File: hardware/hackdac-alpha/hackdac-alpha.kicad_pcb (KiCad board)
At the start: 4 copper layers, 120 x 75 mm, 205 parts, among them J1 VIDEO OUT, J10 HOLE, J11 HOLE, J12 HOLE, J13 HOLE, J2 TTL SYNC, J3 SYNC OUT, J4 I2C, J5 AUDIO OUT, J6 EXT LEDS, J7 EXT POWER, J8 HOLE, J9 HOLE, P1 BANK2_AUX, P2 P22, P3 P28, P4 P20, Q1 2N7002, Q2 BC847, Q3 BC857, Q4 BC857, Q5 2N7002, Q6 2N7002, Q7 IRLML2244, U1 AD768, U10 74LVC1G07, U11 TPS61170DRVR, U12 TPS63700DRCT, U2 MAX4104, U3 TLE2082, U4 MAX4104, U5 MCP47FEB22A1-E/ST, U6 74LVCH16T245, U7 74LVC1G125, U8 MCP1700T-3302E/MB, U9 PCM5102, X1 ECS-TXO-3225-270-TR

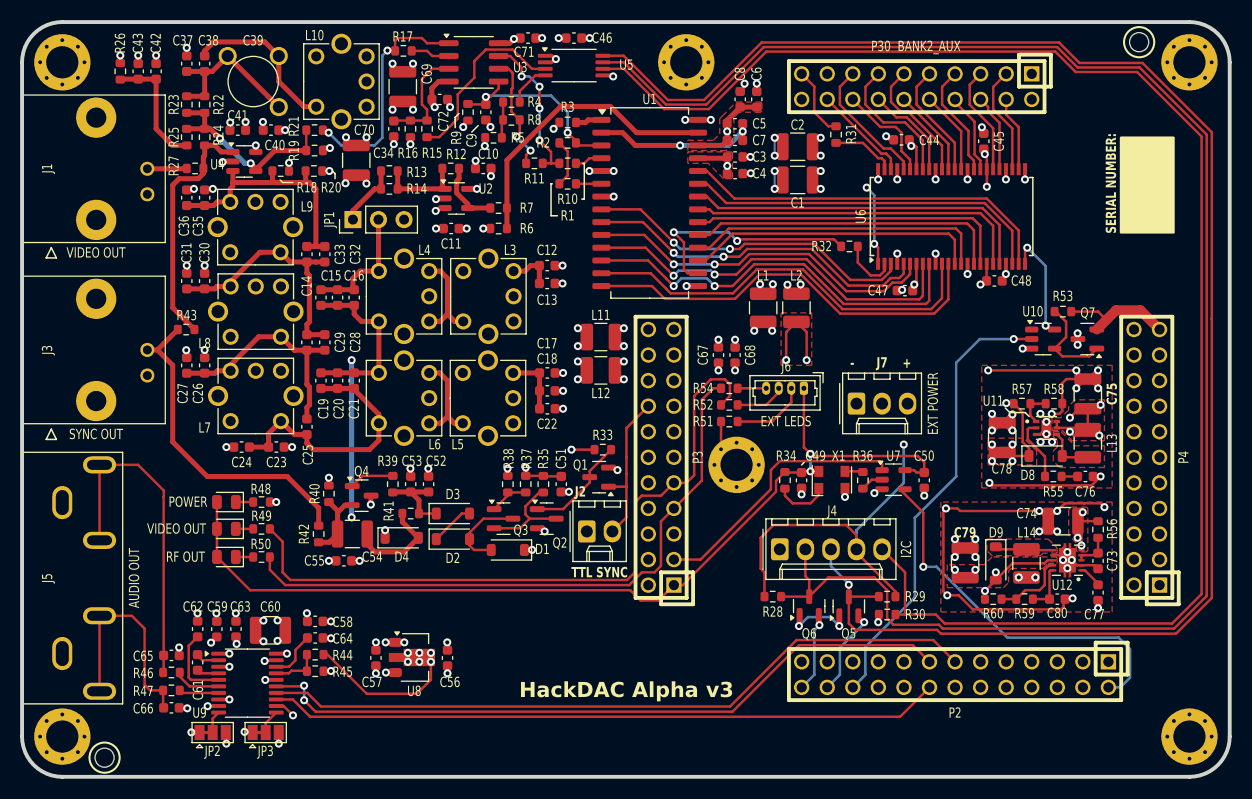
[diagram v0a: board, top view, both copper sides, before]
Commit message: More PCB layout for V3, update readme
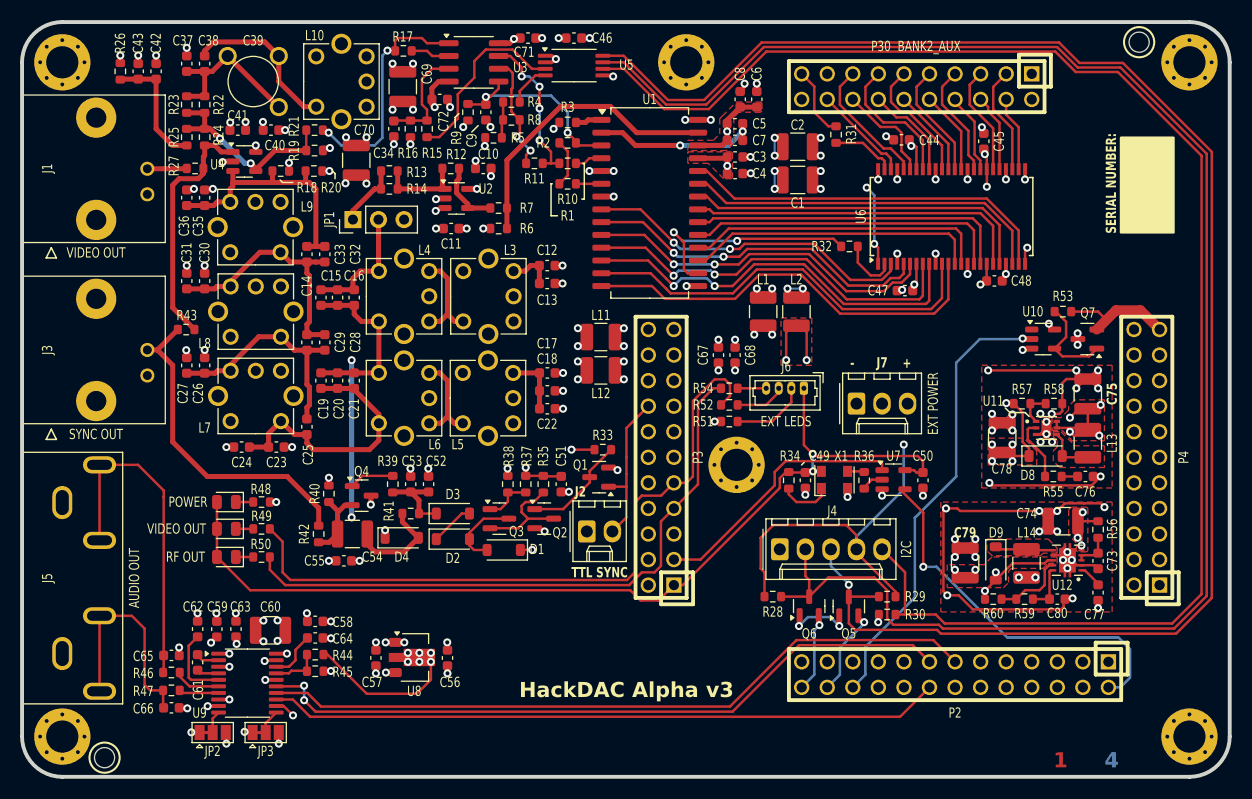
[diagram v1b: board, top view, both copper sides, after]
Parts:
- moved D1 0.41 mm to (127.6, 116.2)
- moved Q3 0.41 mm to (127.1, 113.1)
- moved C49 0.38 mm to (157.5, 109.3)
- moved R34 0.38 mm to (155.9, 109.3)
- moved L1 0.38 mm to (153.4, 92.5)
- moved L2 0.38 mm to (156.7, 92.5)
- moved Q2 0.25 mm to (131.6, 113.1)
- moved X1 0.25 mm to (160.4, 109.2)
- moved C50 0.13 mm to (169.2, 109.3)
- moved R36 0.13 mm to (163.4, 109.3)
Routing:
- net GND: track 1068.2 -> 1071.9 mm, vias 140 -> 141
- net VIN: track 144.8 -> 143.1 mm
- net /video/ADAC-: track 38.1 -> 39.3 mm
- net DA_SDA: track 163.7 -> 162.6 mm
- net DA_HVC: track 151.9 -> 150.8 mm
- net DA_SCL: track 166.6 -> 165.5 mm
- net +5V: track 167.0 -> 168.1 mm
- net /video/ADAC+: track 28.0 -> 29.1 mm
- net Net-(Q3-B): track 4.00 -> 4.78 mm
- net +3.3V_HACKRF: track 291.9 -> 291.2 mm
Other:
- board text added: "1"
- board text added: "2"
- board text added: "3"
- board text added: "4"

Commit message: Modify I2C buffering to allow power-down of HackDAC
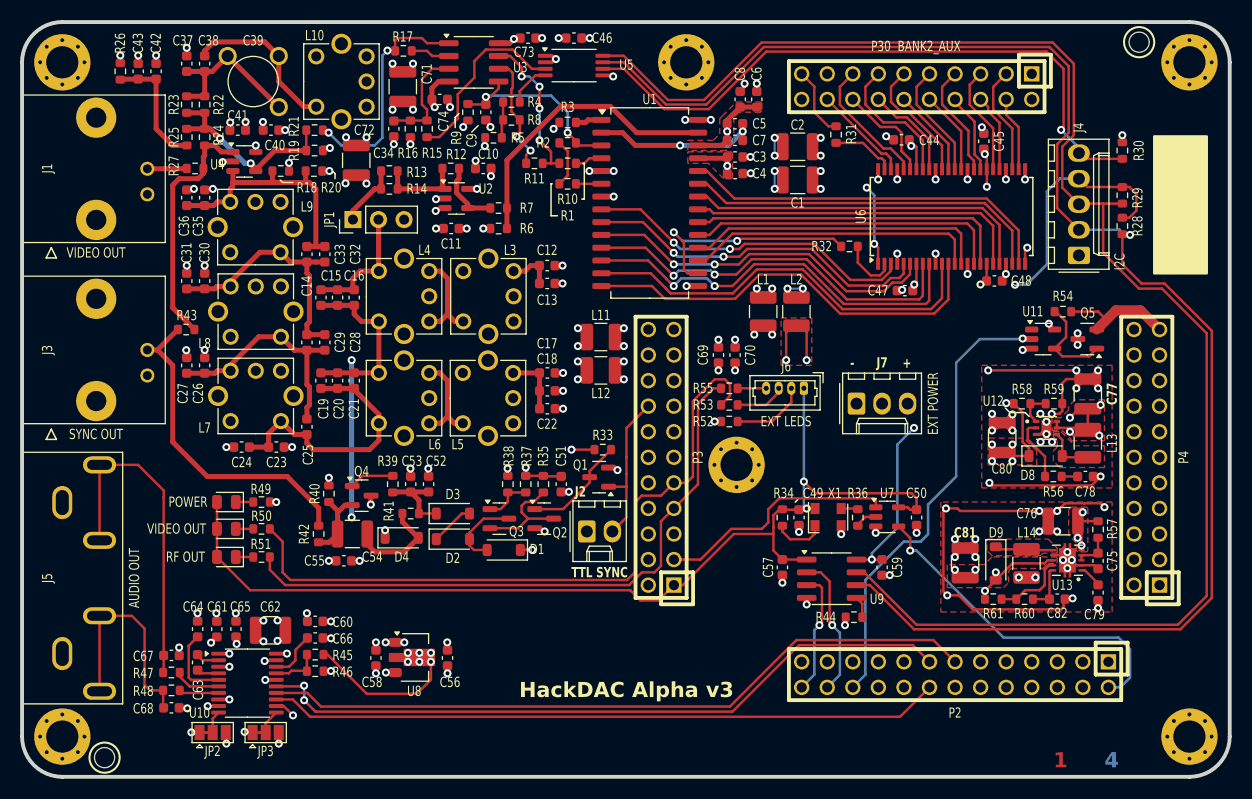
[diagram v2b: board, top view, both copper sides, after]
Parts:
- removed the Q5 at (161.9, 121.8)
- removed Q6: 2N7002, Package_TO_SOT_SMD:SOT-23
- added C57: 100n, Capacitor_SMD:C_0603_1608Metric, F.Cu at (155.3, 117.9)
- added C59: 100n, Capacitor_SMD:C_0603_1608Metric, F.Cu at (165.2, 117.9)
- added R44: NF, Resistor_SMD:R_0603_1608Metric, F.Cu at (162.4, 122.9)
- added U9: TCA9517D, Package_SO:SOIC-8_3.9x4.9mm_P1.27mm, F.Cu at (160.2, 119.1)
- R13, R20: value NF -> 100
- R14, R18: value 50 -> 100
- moved R30 51.7 mm to (189.0, 76.5), turned to 90 degrees
- moved R28 50.6 mm to (189.0, 84.0), turned to -90 degrees
- moved R29 46.2 mm to (189.0, 81.0), turned to -90 degrees
- moved J4 41.7 mm to (184.7, 86.9), turned to 90 degrees
- moved U7 3.75 mm to (165.7, 112.9)
- moved C49 3.75 mm to (156.9, 113.0)
- moved R34 3.75 mm to (155.3, 113.0)
- moved R36 3.75 mm to (162.8, 113.0)
- moved X1 3.75 mm to (159.8, 112.9)
- moved C50 3.75 mm to (168.6, 113.0)
- renumbered C57 to C58, C58 to C60, C59 to C61, C60 to C62, C61 to C63, C62 to C64, C63 to C65, C64 to C66, C65 to C67, C66 to C68, C67 to C69, C68 to C70, C69 to C71, C70 to C72, C71 to C73, C72 to C74, C73 to C75, C74 to C76, C75 to C77, C76 to C78, C77 to C79, C78 to C80, C79 to C81, C80 to C82, Q7 to Q5, R44 to R45, R45 to R46, R46 to R47, R47 to R48, R48 to R49, R49 to R50, R50 to R51, R51 to R52, R52 to R53, R53 to R54, R54 to R55, R55 to R56, R56 to R57, R57 to R58, R58 to R59, R59 to R60, R60 to R61, U9 to U10, U10 to U11, U11 to U12, U12 to U13
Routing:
- net DA_HVC: track 150.8 -> 64.3 mm, vias 0 -> 1
- net GND: track 1071.9 -> 1133.3 mm, vias 141 -> 145
- net DA_SCL: track 165.5 -> 154.5 mm, vias 0 -> 1
- net DA_SDA: track 162.6 -> 154.1 mm, vias 1 -> 0
- net +5V: track 168.1 -> 175.4 mm, vias 15 -> 17
- net /audio/SDA: track 8.87 -> 14.1 mm
- net /audio/SCL: track 7.90 -> 12.5 mm
- net TCXO_CLK: track 38.0 -> 34.7 mm
- net TCXO_ENABLE: track 26.3 -> 24.1 mm
- net Net-(U9-EN): track 0.00 -> 2.16 mm
- net PWR_EN: track 45.0 -> 46.0 mm
- net VIN: track 143.1 -> 143.7 mm
- net +3.3V_HACKRF: track 291.2 -> 291.5 mm, vias 11 -> 9
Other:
- board text removed: "SERIAL NUMBER:"

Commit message: Move LEDs underneath lightpipes
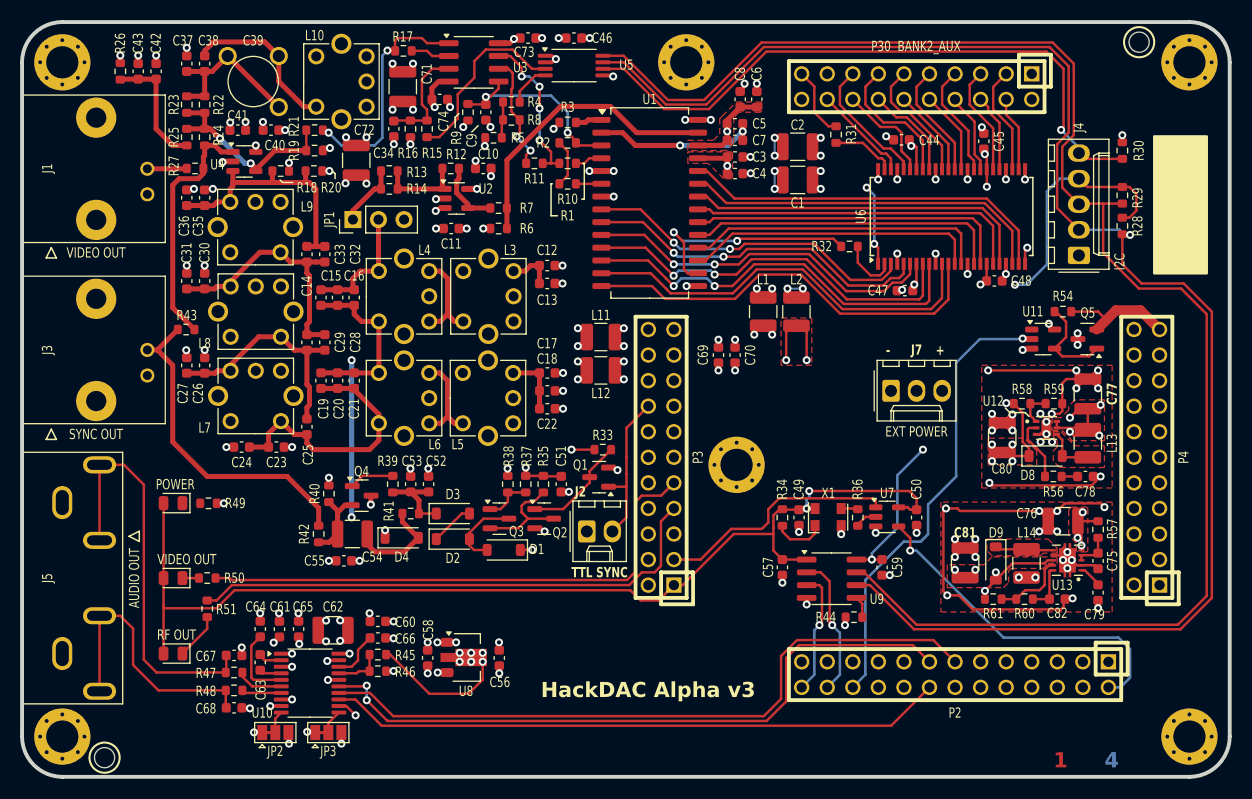
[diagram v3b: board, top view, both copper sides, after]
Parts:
- removed J6: EXT LEDS, Connector_Molex:Molex_PicoBlade_53047-0410_1x04_P1.25mm_Vertical
- removed R52, R53, R55: 100, Resistor_SMD:R_0603_1608Metric
- moved D7 11.0 mm to (94.7, 126.5)
- moved R51 7.46 mm to (98.1, 122.0), turned to -90 degrees
- moved R50 7.28 mm to (98.1, 119.0)
- moved D6 7.21 mm to (94.7, 119.0)
- moved C60 6.22 mm to (115.1, 123.3)
- moved C61 6.22 mm to (105.3, 124.1)
- moved C62 6.22 mm to (110.6, 124.2)
- moved C63 6.22 mm to (103.4, 127.4)
- moved C64 6.22 mm to (103.4, 124.1)
- moved C65 6.22 mm to (107.2, 124.1)
- moved C66 6.22 mm to (115.1, 125.0)
- moved C67 6.22 mm to (100.8, 126.7)
- moved C68 6.22 mm to (100.8, 131.9)
- moved JP2 6.22 mm to (104.9, 134.3)
- moved JP3 6.22 mm to (110.1, 134.3)
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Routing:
- net /power/VIDEO_OUT_LED: track 68.9 -> 53.7 mm
- net /power/RF_OUT_LED: track 62.1 -> 52.8 mm
- net Net-(J6-Pin_2): track 7.52 -> 0.00 mm
- net +5V: track 175.4 -> 168.0 mm
- net Net-(J5-IN2): track 33.1 -> 40.5 mm
- net GND: track 1133.3 -> 1139.6 mm, vias 145 -> 144
- net /audio/I2S_SCK: track 66.8 -> 61.3 mm
- net Net-(J5-IN1): track 21.9 -> 27.0 mm
- net Net-(J6-Pin_3): track 5.00 -> 0.00 mm
- net -5V: track 66.1 -> 70.3 mm
- net +3.3V_HACKRF: track 291.5 -> 294.7 mm
- net /audio/I2S_SDA: track 71.6 -> 68.7 mm
- net /audio/I2S_WS: track 70.3 -> 67.4 mm
- net Net-(D7-K): track 1.73 -> 4.65 mm
- net Net-(J6-Pin_4): track 2.83 -> 0.00 mm
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
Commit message: Changed X1 to 5x3.2mm footprint
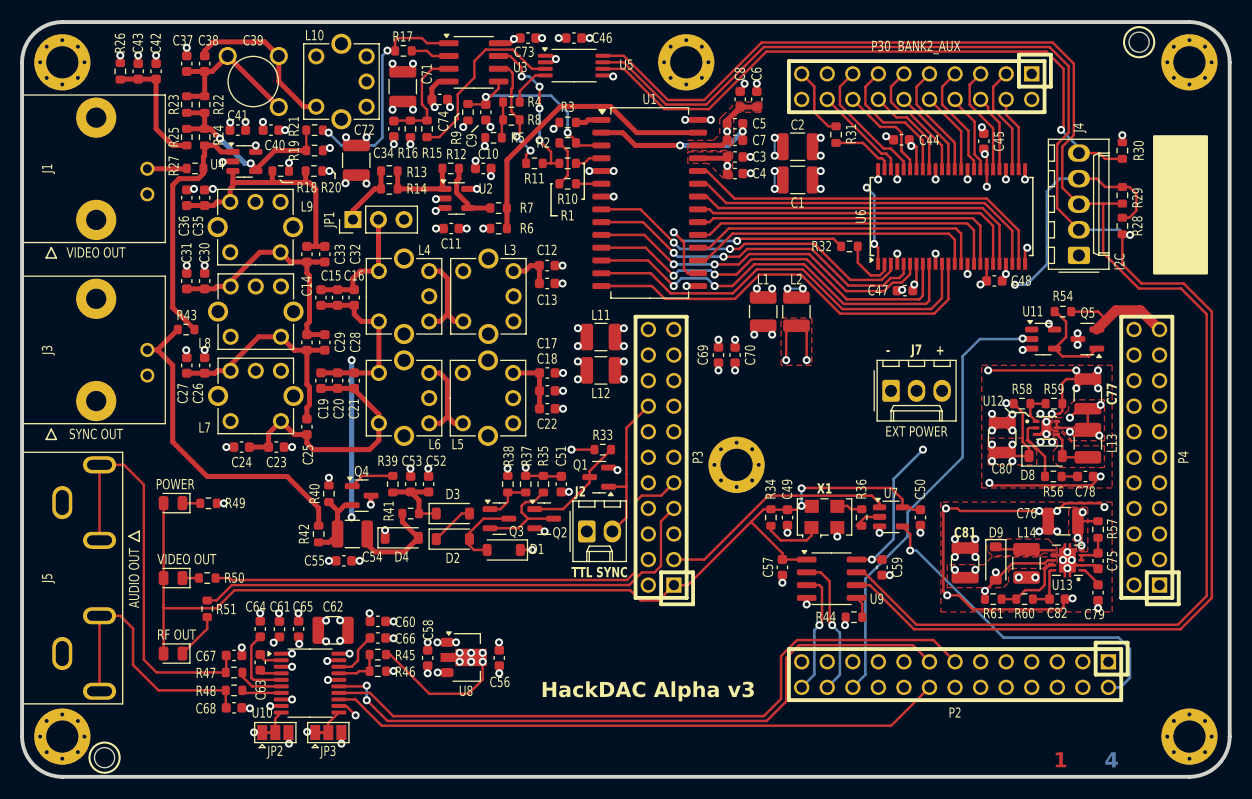
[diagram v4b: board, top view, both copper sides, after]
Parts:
- X1: footprint Oscillator:Oscillator_SMD_EuroQuartz_XO32-4Pin_3.2x2.5mm -> Oscillator:Oscillator_SMD_EuroQuartz_XO53-4Pin_5.0x3.2mm
- moved R34 1.15 mm to (154.1, 113.0)
- moved C49 1.15 mm to (155.8, 113.0)
- moved U7 0.38 mm to (166.1, 112.9)
- moved C50 0.38 mm to (169.0, 113.0)
- moved R36 0.38 mm to (163.1, 113.0)
- moved X1 0.35 mm to (159.5, 112.9), turned to 0 degrees
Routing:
- net VIN: track 141.3 -> 138.4 mm
- net Net-(D5-K): track 0.00 -> 1.77 mm
- net +3.3V_HACKRF: track 294.7 -> 295.8 mm
- net PWR_EN: track 46.0 -> 45.0 mm
- net Net-(X1-EN): track 5.14 -> 5.87 mm
- net TCXO_CLK: track 34.7 -> 34.0 mm

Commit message: Add jumper to configure sync out connector
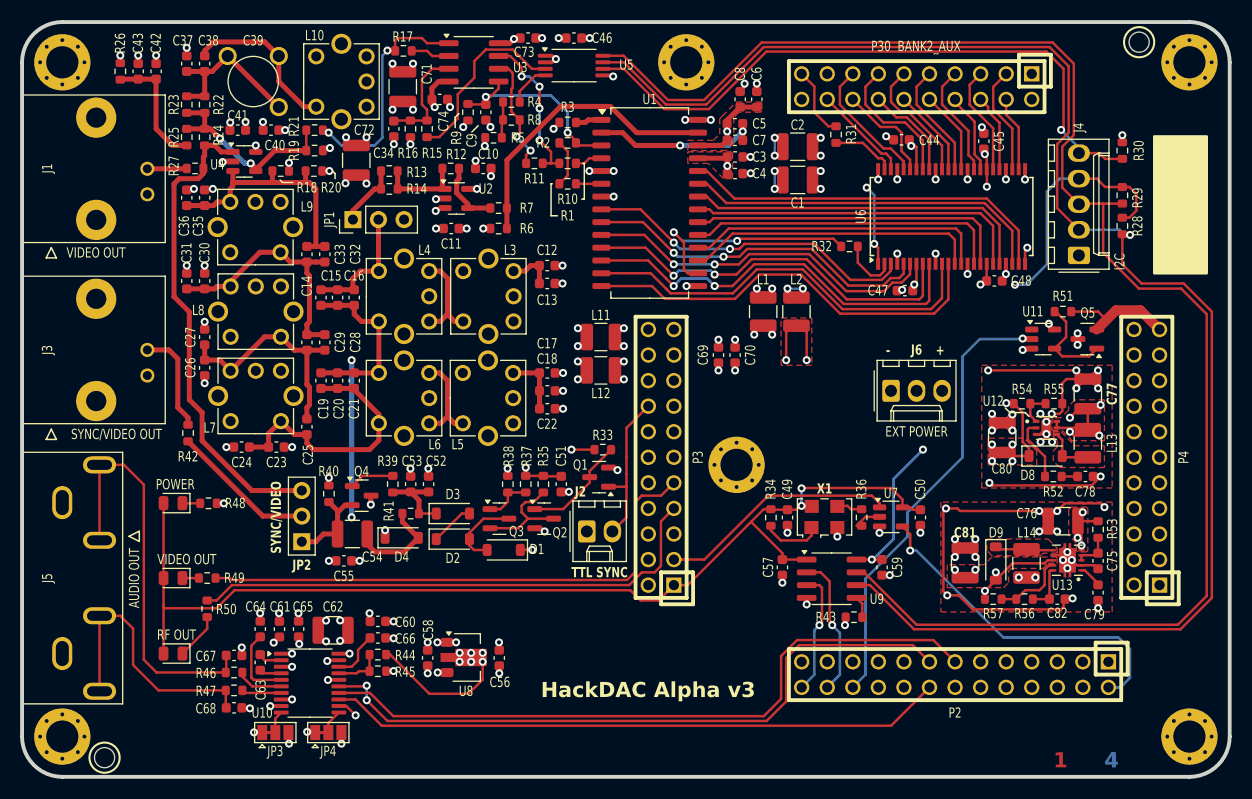
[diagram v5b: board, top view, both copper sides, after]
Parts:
- removed the R43 at (96.0, 94.3)
- added JP2: SYNC/VIDEO, Connector_PinHeader_2.54mm:PinHeader_1x03_P2.54mm_Vertical, F.Cu at (107.5, 115.4)
- J3: value SYNC OUT -> SYNC/VIDEO OUT
- R34: value 10k -> NF
- X1: value ECS-TXO-3225-270-TR -> ECS-5032MV-270-CN-TR
- moved R42 16.4 mm to (96.2, 104.6)
- moved C27 3.33 mm to (97.9, 95.0)
- moved C26 0.24 mm to (97.9, 98.1), turned to -90 degrees
- renumbered J11 to J10, J12 to J11, J13 to J12, J7 to J6, J8 to J7, J9 to J8, J10 to J9, JP2 to JP3, JP3 to JP4, R44 to R43, R45 to R44, R46 to R45, R47 to R46, R48 to R47, R49 to R48, R50 to R49, R51 to R50, R54 to R51, R56 to R52, R57 to R53, R58 to R54, R59 to R55, R60 to R56, R61 to R57
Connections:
- C54 pad 1: Net-(Q4-E) -> Net-(JP2-A)
- Q4 pad 2: Net-(Q4-E) -> Net-(JP2-A)
- R40 pad 2: Net-(Q4-E) -> Net-(JP2-A)
- R42 pad 1: Net-(Q4-E) -> Net-(JP2-C)
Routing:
- net VIDEO: track 24.7 -> 47.9 mm
- net Net-(J3-In): track 32.6 -> 10.4 mm
- net Net-(JP2-C): track 0.00 -> 14.4 mm
- net Net-(JP2-A): track 0.00 -> 9.16 mm
- net Net-(Q4-E): track 7.51 -> 0.00 mm
- net GND: track 1139.5 -> 1137.0 mm
